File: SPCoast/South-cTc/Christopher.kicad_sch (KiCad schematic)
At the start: 1 part

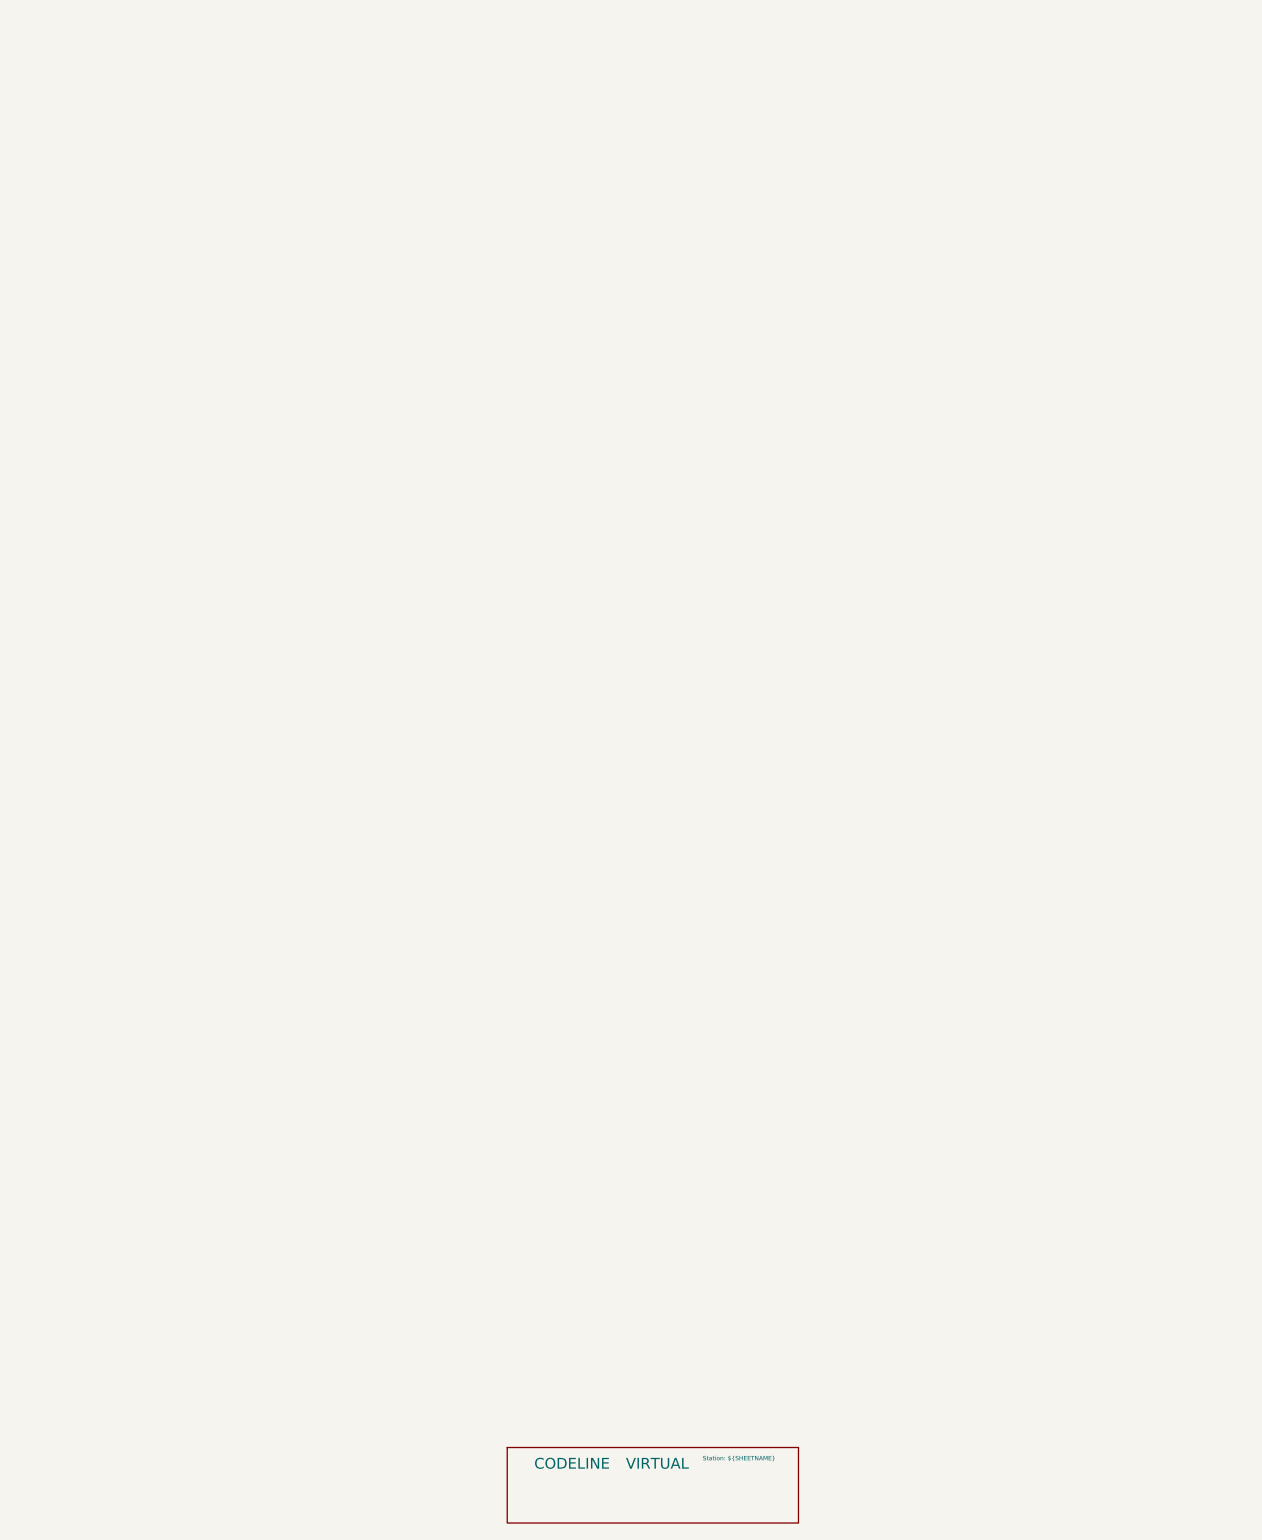
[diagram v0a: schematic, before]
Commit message: SPCoast: derail pin R, track circuit names end in T, code line symbols on the root sheet
Working-tree changes from the 2026-10-01..03 vocabulary review with
FieldUnit-Subdivision (docs/adr/0001-code-line-type-contract.md):

- Switch_Powered_Derail pin 2 is R (through path = REVERSE) in the seven
  plant schematics (library Railroad.kicad_sym renamed alongside; not in git)
- Luchessa track circuits renamed to end in T (1SAT, 2NAAT, ...); MC1 moved
  to CP Gilroy's house
- South-cTc: transports (MQTT, TimeCode, CMRInet, Loconet) on the root
  sheet on the CtcMachine Transports pin; field stations as encoding
  instances on the Luchessa sheet; two Luchessa lamp tokens renamed
- Six plant projects (Christopher, Corporal, GilroyCalTrain,
  GilroyInterchange, Sargent, Watsonville) added as drawn so far; Watsonville
  updated 2026-10-02

Co-Authored-By: Claude Fable 5.1 <noreply@anthropic.com>
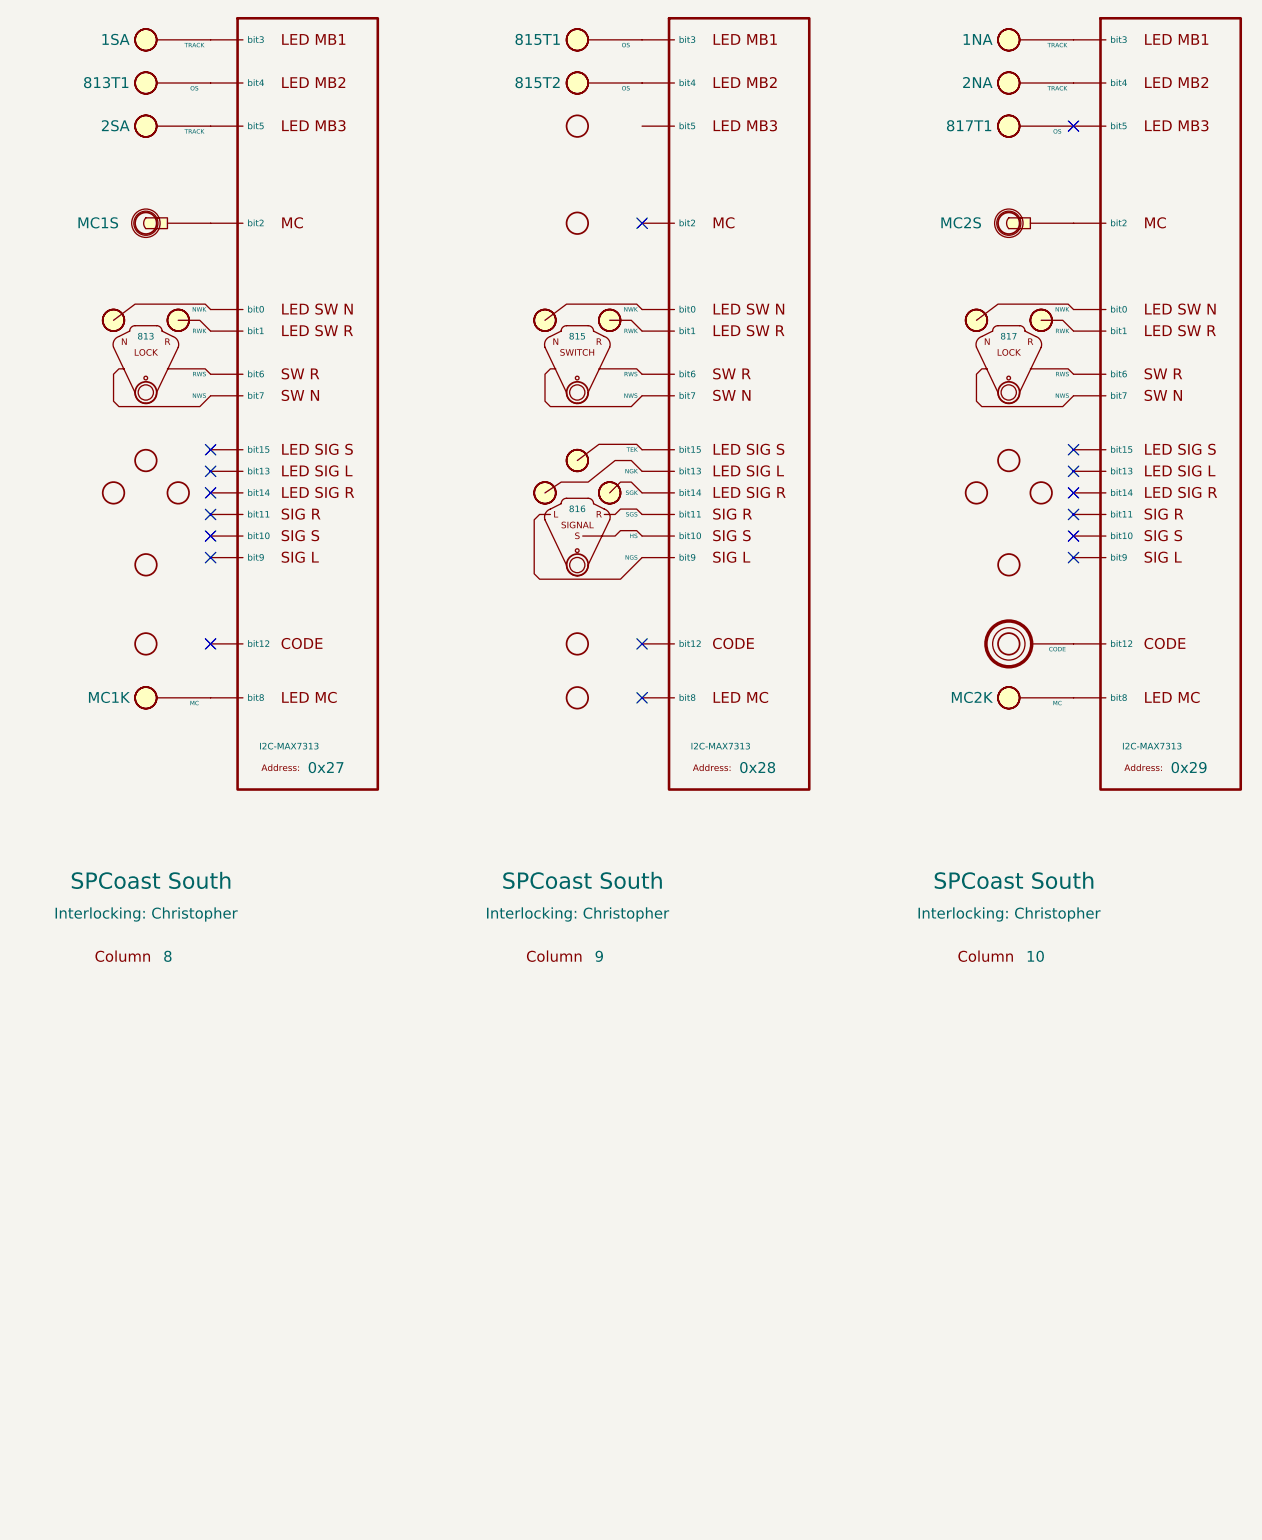
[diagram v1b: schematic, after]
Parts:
- removed CODELINE4: VIRTUAL, symbol RailroadPanel:Codeline-Virtual
- added CDE10: CODE, symbol RailroadPanel:PanelCode
- added COL28: 8, symbol RailroadPanel:PanelColumn
- added COL29: 9, symbol RailroadPanel:PanelColumn
- added COL30: 10, symbol RailroadPanel:PanelColumn
- added LKL10: 817, symbol RailroadPanel:PanelLock
- added LKL8: 813, symbol RailroadPanel:PanelLock
- added LMP101, LMP102, LMP81, LMP83: TRACK, symbol RailroadPanel:PanelLamp-YELLOW
- added LMP82, LMP93: OS, symbol RailroadPanel:PanelLamp-YELLOW
- added LMP91, LMP92: OS, symbol RailroadPanel:PanelLamp-RED
- added MCK10, MCK8: MC, symbol RailroadPanel:PanelLamp-YELLOW
- added MCL10: MC2, symbol RailroadPanel:PanelMCall
- added MCL8: MC1, symbol RailroadPanel:PanelMCall
- added SGL9: 816, symbol RailroadPanel:PanelSignal
- added SWL9: 815, symbol RailroadPanel:PanelSwitch
- added U28: 0x27, symbol RailroadPanel:PanelColumn-MAX7313
- added U29: 0x28, symbol RailroadPanel:PanelColumn-MAX7313
- added U30: 0x29, symbol RailroadPanel:PanelColumn-MAX7313
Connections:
- new net: COL29.6 (Column), SGL9.1 (Column)
- new net: SGL9.2 (NGS), U29.10 (bit9)
- new net: SGL9.3 (HS), U29.11 (bit10)
- new net: SGL9.4 (SGS), U29.12 (bit11)
- new net: SGL9.5 (SGK), U29.15 (bit14)
- new net: SGL9.6 (NGK), U29.14 (bit13)
- new net: SGL9.7 (TEK), U29.16 (bit15)
- new net: SWL9.5 (NWK), U29.1 (bit0)
- new net: SWL9.4 (RWK), U29.2 (bit1)
- new net: LMP91.2 (LAMP), U29.4 (bit3)
- new net: LMP92.2 (LAMP), U29.5 (bit4)
- new net: SWL9.3 (RWS), U29.7 (bit6)
- new net: SWL9.2 (NWS), U29.8 (bit7)
- new net: COL30.8 (Column), MCK10.1 (Column)
- new net: MCK10.2 (LAMP), U30.9 (bit8)
- new net: COL29.1 (Column), LMP91.1 (Column)
- new net: COL30.2 (Column), LMP102.1 (Column)
- new net: LMP102.2 (LAMP), U30.5 (bit4)
- new net: COL28.3 (Column), LMP83.1 (Column)
- new net: LMP83.2 (LAMP), U28.6 (bit5)
- new net: LKL10.5 (NWK), U30.1 (bit0)
- new net: CDE10.2 (CODE), U30.13 (bit12)
- new net: LKL10.4 (RWK), U30.2 (bit1)
- new net: MCL10.2 (SW), U30.3 (bit2)
- new net: LMP101.2 (LAMP), U30.4 (bit3)
- new net: LMP93.2 (LAMP), U30.6 (bit5)
- new net: LKL10.3 (RWS), U30.7 (bit6)
- new net: LKL10.2 (NWS), U30.8 (bit7)
- new net: COL28.5 (Column), LKL8.1 (Column)
- new net: LKL8.2 (NWS), U28.8 (bit7)
- new net: LKL8.3 (RWS), U28.7 (bit6)
- new net: LKL8.4 (RWK), U28.2 (bit1)
- new net: LKL8.5 (NWK), U28.1 (bit0)
- new net: COL30.3 (Column), LMP93.1 (Column)
- new net: COL28.2 (Column), LMP82.1 (Column)
- new net: LMP82.2 (LAMP), U28.5 (bit4)
- new net: COL30.1 (Column), LMP101.1 (Column)
- new net: COL30.4 (Column), MCL10.1 (Column)
- new net: COL30.5 (Column), LKL10.1 (Column)
- new net: CDE10.1 (Column), COL30.7 (Column)
- new net: COL28.1 (Column), LMP81.1 (Column)
- new net: LMP81.2 (LAMP), U28.4 (bit3)
- new net: COL29.2 (Column), LMP92.1 (Column)
- new net: COL29.5 (Column), SWL9.1 (Column)
- new net: MCL8.2 (SW), U28.3 (bit2)
- new net: MCK8.2 (LAMP), U28.9 (bit8)
- new net: COL28.8 (Column), MCK8.1 (Column)
- new net: COL28.4 (Column), MCL8.1 (Column)
- no-connect marks 0 -> 17

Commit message: SPCoast: Address field and Kind on PanelColumn-MAX7313; encoding Values; HBA; Watsonville update
Owner's drawing changes of 2026-10-02..03 (FieldUnit-Subdivision ADR 0002 D18
and the owner's responses):

- PanelColumn-MAX7313: the expander address moves from the Value to an
  Address field (Value is ${Address}); BusKind renamed Kind (I2C-MAX7313)
- Luchessa encoding symbols: Value "US&S 506 time-coded DC pulses"
- Sargent: HBD renamed HBA; traffic indications [NSEW]FLK
- Watsonville schematic brought to a usable state
- Luchessa plant: track circuits end in T; MC1 at CP Gilroy's house

Co-Authored-By: Claude Fable 5.1 <noreply@anthropic.com>
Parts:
- U28: Address (none) -> 0x27; BusKind I2C-MAX7313 -> (none); Kind (none) -> I2C-MAX7313
- U29: Address (none) -> 0x28; BusKind I2C-MAX7313 -> (none); Kind (none) -> I2C-MAX7313
- U30: Address (none) -> 0x29; BusKind I2C-MAX7313 -> (none); Kind (none) -> I2C-MAX7313
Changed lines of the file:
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@@
 		(property "Value" "0x28"
 			(at 149.86 112.395 0)
+			(hide yes)
 			(show_name no)
 			(do_not_autoplace yes)
@@
 			)
 		)
-		(property "BusKind" "I2C-MAX7313"
+		(property "Role" "IODRIVER"
+			(at 148.59 107.315 0)
+			(hide yes)
+			(show_name no)
+			(do_not_autoplace no)
+			(effects
+				(font
+					(size 1.27 1.27)
+				)
+			)
+		)
+		(property "Kind" "I2C-MAX7313"
 			(at 144.145 109.855 0)
 			(show_name no)
-			(do_not_autoplace yes)
+			(do_not_autoplace no)
 			(effects
 				(font
@@
 			)
 		)
-		(property "Role" "IODRIVER"
-			(at 149.86 72.39 0)
-			(hide yes)
+		(property "Address" "0x28"
+			(at 152.146 112.522 0)
 			(show_name no)
 			(do_not_autoplace no)
@@
 		(property "Value" "0x29"
 			(at 200.66 112.395 0)
+			(hide yes)
 			(show_name no)
 			(do_not_autoplace yes)
@@
 			)
 		)
-		(property "BusKind" "I2C-MAX7313"
+		(property "Role" "IODRIVER"
+			(at 199.39 107.315 0)
+			(hide yes)
+			(show_name no)
+			(do_not_autoplace no)
+			(effects
+				(font
+					(size 1.27 1.27)
+				)
+			)
+		)
+		(property "Kind" "I2C-MAX7313"
 			(at 194.945 109.855 0)
 			(show_name no)
-			(do_not_autoplace yes)
+			(do_not_autoplace no)
 			(effects
 				(font
@@
 			)
 		)
-		(property "Role" "IODRIVER"
-			(at 200.66 72.39 0)
-			(hide yes)
+		(property "Address" "0x29"
+			(at 202.946 112.268 0)
 			(show_name no)
 			(do_not_autoplace no)
@@
 		(property "Value" "0x27"
 			(at 99.06 112.395 0)
+			(hide yes)
 			(show_name no)
 			(do_not_autoplace yes)
@@
 			)
 		)
-		(property "BusKind" "I2C-MAX7313"
+		(property "Role" "IODRIVER"
+			(at 97.79 107.315 0)
+			(hide yes)
+			(show_name no)
+			(do_not_autoplace no)
+			(effects
+				(font
+					(size 1.27 1.27)
+				)
+			)
+		)
+		(property "Kind" "I2C-MAX7313"
 			(at 93.345 109.855 0)
 			(show_name no)
-			(do_not_autoplace yes)
+			(do_not_autoplace no)
 			(effects
 				(font
@@
 			)
 		)
-		(property "Role" "IODRIVER"
-			(at 99.06 72.39 0)
-			(hide yes)
-			(show_name no)
-			(do_not_autoplace no)
+		(property "Address" "0x27"
+			(at 101.092 112.268 0)
+			(show_name no)
+			(do_not_autoplace no)

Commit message: fix(kicad): approach circuits end in T; desk tokens follow
Plants: Christopher 1NA/2NA/1SA/2SA, GilroyCalTrain 1NA/1SA, GilroyInterchange
1SA, Sargent 1NA/1SA/2SA gain the final T (ADR 0003 D4). Sargent's reference
Corporal:2NA becomes Corporal:2NAT, the circuit Corporal draws.

Desk (South-cTc sheets): IndicationToken follows the plants for Christopher,
GilroyCalTrain, GilroyInterchange; Corporal 1SA becomes 1SAT (the plant already
had it); Christopher 815T2 becomes 815AT1 (the OS circuit of switch 815A).

Not changed, awaiting decisions in the dry-run report: 0<n>T renames (IND,
TK<n>, Interchange, 2NAAT, 2SAT), section 2 of an approach, unnamed circuits,
Watsonville, CP_Watsonville: references, 1TK.

Verified: netlists rebuilt for all affected projects; of 33 desk circuit tokens,
5 now match no plant circuit (was 11): 1TK, CP_Watsonville:SA1,
CP_Watsonville:837T1, Watsonville 1NAK and 2NAK. KiCad closed, no ~*.lck.

Co-Authored-By: Claude Sonnet 5.5 <noreply@anthropic.com>
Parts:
- LMP101: IndicationToken 1NA -> 1NAT
- LMP102: IndicationToken 2NA -> 2NAT
- LMP81: IndicationToken 1SA -> 1SAT
- LMP83: IndicationToken 2SA -> 2SAT
- LMP92: IndicationToken 815T2 -> 815AT1
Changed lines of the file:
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@@
 			)
 		)
-		(property "IndicationToken" "2NA"
+		(property "IndicationToken" "2NAT"
 			(at 179.705 31.75 0)
 			(show_name no)
@@
 			)
 		)
-		(property "IndicationToken" "2SA"
+		(property "IndicationToken" "2SAT"
 			(at 78.105 36.83 0)
 			(show_name no)
@@
 			)
 		)
-		(property "IndicationToken" "1SA"
+		(property "IndicationToken" "1SAT"
 			(at 78.105 26.67 0)
 			(show_name no)
@@
 			)
 		)
-		(property "IndicationToken" "815T2"
+		(property "IndicationToken" "815AT1"
 			(at 128.905 31.75 0)
 			(show_name no)
@@
 			)
 		)
-		(property "IndicationToken" "1NA"
+		(property "IndicationToken" "1NAT"
 			(at 179.705 26.67 0)
 			(show_name no)
